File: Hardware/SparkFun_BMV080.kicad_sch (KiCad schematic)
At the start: 24 parts, among them J1 Qwiic_RA, J2 Conn_01x07, U1 BMV080

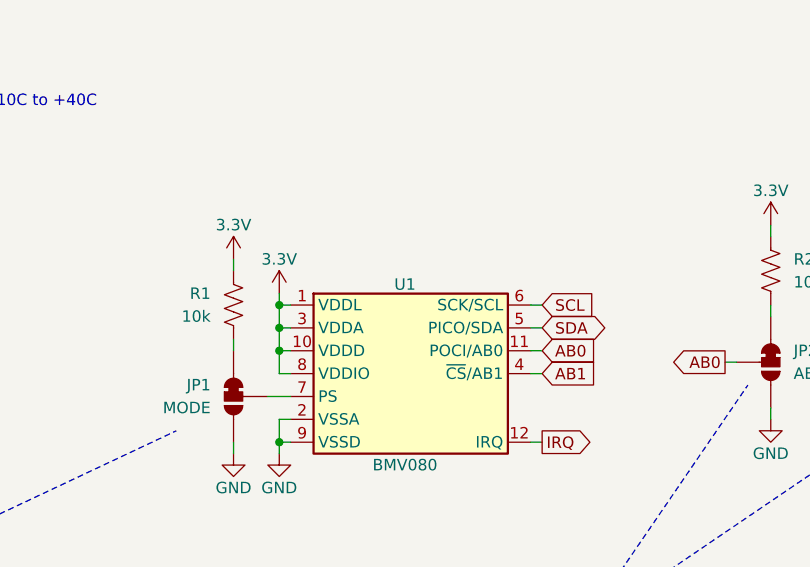
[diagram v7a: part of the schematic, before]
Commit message: library work
-moved bmv080 sensor symbol and footprint to sparkfun libraries with pending PR.
-updated symbol and footprints in kicad design files
-note, the sensor itself and the FPC connector are now separate things. The BMV080 has an "outline" footprint that is placed at the same origin point as the sensor (and includes the 3d model of the sensor itself)
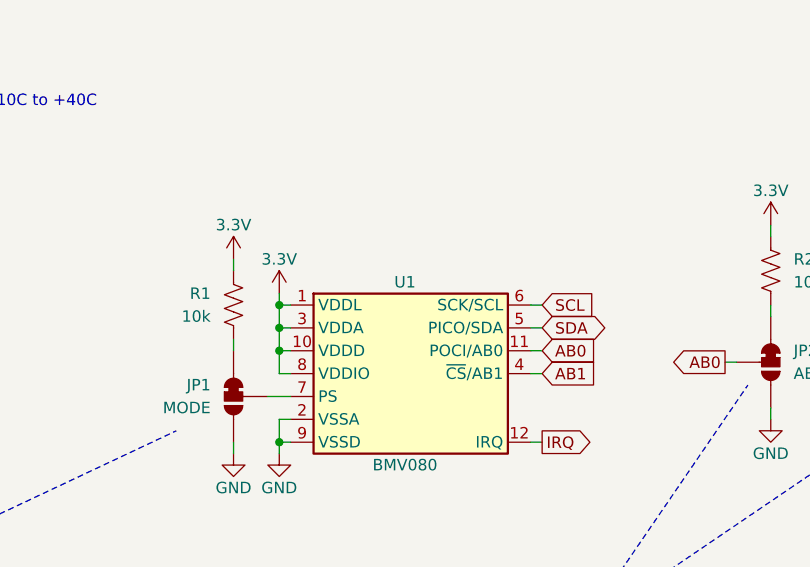
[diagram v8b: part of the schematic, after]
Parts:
- removed U1: BMV080, BMV080:FPC_0.3mm-13_molex_503566-1302, symbol BMV080:BMV080
- added U1: BMV080, SparkFun-Connector:FPC_0.3mm-13, symbol SparkFun-Sensor:BMV080
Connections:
- net 3.3V: now also U1.1 (VDDL), U1.10 (VDDD), U1.3 (VDDA), U1.8 (VDDIO)
- net AB0: now also U1.11 (POCI/AB0)
- net AB1: now also U1.4 (~{CS}/AB1)
- net GND: now also U1.2 (VSSA), U1.9 (VSSD)
- net IRQ: now also U1.12 (IRQ)
- net SCL: now also U1.6 (SCK/SCL)
- net SDA: now also U1.5 (PICO/SDA)
- net at JP1.2 (C): now also U1.7 (PS)
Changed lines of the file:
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@@
-	)
-	(symbol
-		(lib_id "BMV080:BMV080")
-		(at 90.17 68.58 0)
-		(unit 1)
-		(exclude_from_sim no)
-		(in_bom yes)
-		(on_board yes)
-		(dnp no)
-		(property "Reference" "U1"
-			(at 90.17 58.674 0)
-			(effects
-				(font
-					(size 1.27 1.27)
-				)
-			)
-		)
-		(property "Value" "BMV080"
-			(at 90.17 78.74 0)
-			(effects
-				(font
-					(size 1.27 1.27)
-				)
-			)
-		)
-		(property "Footprint" "BMV080:FPC_0.3mm-13_molex_503566-1302"
-			(at 89.662 85.598 0)
-			(effects
-				(font
-					(size 1.27 1.27)
-				)
-				(hide yes)
-			)
-		)
-		(property "Datasheet" "NDA"
-			(at 89.408 83.566 0)
-			(effects
-				(font
-					(size 1.27 1.27)
-				)
-				(hide yes)
-			)
-		)
-		(property "Description" "BMV080 Particulate Matter Sensor"
-			(at 91.44 88.138 0)
-			(effects
-				(font
-					(size 1.27 1.27)
-				)
-				(hide yes)
-			)
-		)
-		(property "PROD_ID" "CONN-22959"
-			(at 90.424 90.17 0)
-			(effects
-				(font
-					(size 1.27 1.27)
-				)
-				(hide yes)
-			)
-		)
-		(property "PROD_ID_SENSOR" "IC-22926"
-			(at 89.662 81.28 0)
-			(effects
-				(font
-					(size 1.27 1.27)
-				)
-				(hide yes)
-			)
-		)
-		(pin "6"
-		)
-		(pin "9"
-		)
-		(pin "11"
-		)
-		(pin "1"
-		)
-		(pin "5"
-		)
-		(pin "12"
-		)
-		(pin "10"
-		)
-		(pin "7"
-		)
-		(pin "13"
-		)
-		(pin "2"
-		)
-		(pin "4"
-		)
-		(pin "3"
-		)
-		(pin "8"
-		)
-		(instances
-			(project ""
-				(path "/7d38b1bd-099f-4b8c-8c99-a0900e0f5fdd"
-					(reference "U1")
-					(unit 1)
-				)
-			)
-		)
 	)
 	(symbol
@@
 					(unit 1)
 				)
+			)
+		)
+	)
+	(symbol
+		(lib_id "SparkFun-Sensor:BMV080")
+		(at 90.17 68.58 0)
+		(unit 1)
+		(exclude_from_sim no)
+		(in_bom yes)
+		(on_board yes)
+		(dnp no)
+		(property "Reference" "U1"
+			(at 90.17 58.42 0)
+			(effects
+				(font
+					(size 1.27 1.27)
+				)
+			)
+		)
+		(property "Value" "BMV080"
+			(at 90.17 78.74 0)
+			(effects
+				(font
+					(size 1.27 1.27)
+				)
+			)
+		)
+		(property "Footprint" "SparkFun-Connector:FPC_0.3mm-13"
+			(at 89.662 85.598 0)
+			(effects
+				(font
+					(size 1.27 1.27)
+				)
+				(hide yes)
+			)
+		)
+		(property "Datasheet" "https://www.bosch-sensortec.com/media/boschsensortec/downloads/datasheets/bst-bmv080-ds000.pdf"
+			(at 89.408 83.566 0)
+			(effects
+				(font
+					(size 1.27 1.27)
+				)
+				(hide yes)
+			)
+		)
+		(property "Description" "BMV080 Particulate Matter Sensor"
+			(at 91.44 88.138 0)
+			(effects
+				(font
+					(size 1.27 1.27)
+				)
+				(hide yes)
+			)
+		)
+		(property "PROD_ID" "CONN-22959"
+			(at 90.424 90.17 0)
+			(effects
+				(font
+					(size 1.27 1.27)
+				)
+				(hide yes)
+			)
+		)
+		(property "PROD_ID_SENSOR" "IC-22926"
+			(at 89.662 81.28 0)
+			(effects
+				(font
+					(size 1.27 1.27)
+				)
+				(hide yes)
+			)
+		)
+		(pin "5"
+		)
+		(pin "12"
+		)
+		(pin "4"
+		)
+		(pin "6"
+		)
+		(pin "8"
+		)
+		(pin "9"
+		)
+		(pin "11"
+		)
+		(pin "1"
+		)
+		(pin "13"
+		)
+		(pin "3"
+		)
+		(pin "7"
+		)
+		(pin "10"
+		)
+		(pin "2"
+		)
+		(instances
+			(project ""
+				(path "/7d38b1bd-099f-4b8c-8c99-a0900e0f5fdd"
+					(reference "U1")
+					(unit 1)
+				)
